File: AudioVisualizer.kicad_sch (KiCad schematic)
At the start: 327 parts, among them J1 AudioJack3, J2 AudioJack3, J3 Screw_Terminal_01x03, J4 USB_A, U1 LM2904, U10 LM393, U11 LM393, U12 LM393, U13 LM393, U14 LM393, U15 LM393, U16 LM393, U17 LM393, U18 LM393, U19 LM393, U2 LM2904, U20 LM393, U21 LM393, U22 LM393, U23 LM393, U24 LM393, U25 LM393, U26 LM393, U27 LM393, U28 LM393, U29 LM393, U3 LM2904, U30 LM393, U31 LM393, U32 LM393, U33 LM393, U34 LM393, U35 LM393, U36 LM393, U37 LM393, U38 LM393, U39 LM393, U4 LM2904, U40 LM393, U41 LM393, U42 LM393, U43 LM393, U44 LM393, U45 LM393, U46 LM393, U47 LM393, U48 LM393, U49 LM393, U5 LM2904, U50 LM393, U51 LM393, U52 LM393, U53 LM393, U54 L7805, U55 L7805, U6 LM393, U7 LM393, U8 LM393, U9 LM393

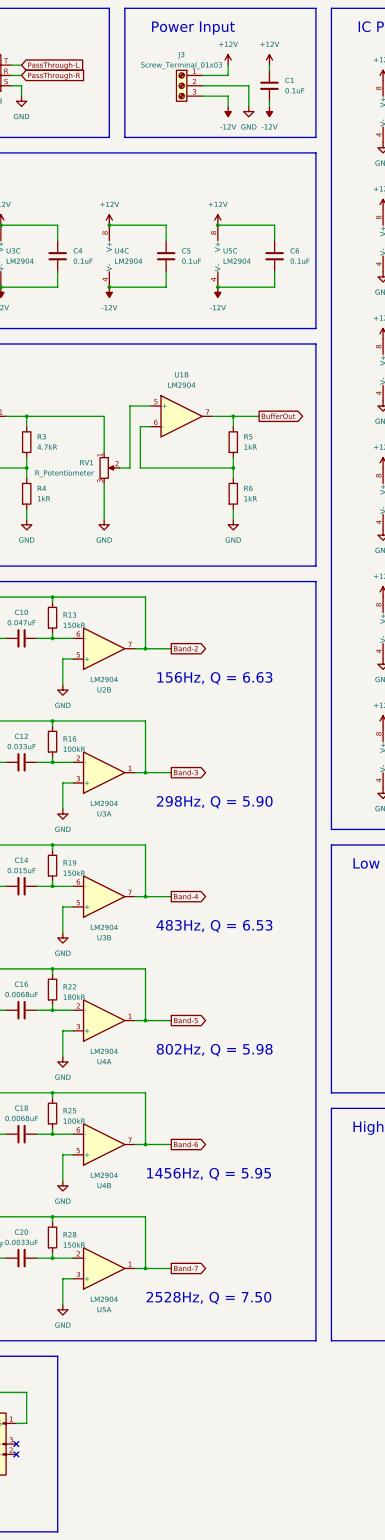
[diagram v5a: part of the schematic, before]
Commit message: 電源入力のパスコンを削除
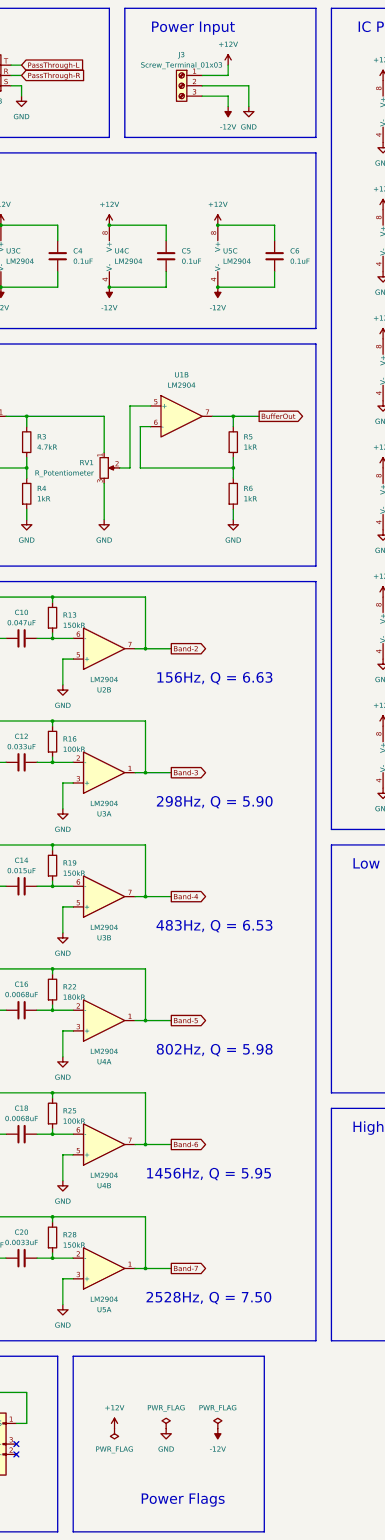
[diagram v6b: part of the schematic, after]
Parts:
- removed C1: 0.1uF, Capacitor_THT:C_Disc_D5.0mm_W2.5mm_P5.00mm, symbol Device:C
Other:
- note added: "Power Flags"
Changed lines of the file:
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@@
     (stroke (width 0) (type default))
   )
-  (wire (pts (xy 389.89 36.83) (xy 389.89 38.1))
-    (stroke (width 0) (type default))
-  )
   (wire (pts (xy 64.77 295.91) (xy 69.85 295.91))
     (stroke (width 0) (type default))
@@
     (stroke (width 0) (type default))
   )
-  (wire (pts (xy 389.89 45.72) (xy 389.89 46.99))
-    (stroke (width 0) (type default))
-  )
   (wire (pts (xy 538.48 170.18) (xy 558.8 170.18))
     (stroke (width 0) (type default))
@@
     (fill (type none))
   )
+  (rectangle (start 341.63 354.33) (end 388.62 397.51)
+    (stroke (width 0) (type default))
+    (fill (type none))
+  )
   (rectangle (start 265.43 354.33) (end 337.82 397.51)
     (stroke (width 0) (type default))
@@
     (effects (font (size 2.54 2.54)) (justify left bottom))
   )
+  (text "Power Flags" (at 358.14 391.16 0)
+    (effects (font (size 2.54 2.54)) (justify left bottom))
+  )
   (text "802Hz, Q = 5.98" (at 361.95 280.67 0)
     (effects (font (size 2.54 2.54)) (justify left bottom))
@@
     )
   )
+  (symbol (lib_id "power:GND") (at 364.49 372.11 0) (unit 1)
+    (in_bom yes) (on_board yes) (dnp no) (fields_autoplaced)
+    (property "Reference" "#PWR010" (at 364.49 378.46 0)
+      (effects (font (size 1.27 1.27)) hide)
+    )
+    (property "Value" "GND" (at 364.49 377.19 0)
+      (effects (font (size 1.27 1.27)))
+    )
+    (property "Footprint" "" (at 364.49 372.11 0)
+      (effects (font (size 1.27 1.27)) hide)
+    )
+    (property "Datasheet" "" (at 364.49 372.11 0)
+      (effects (font (size 1.27 1.27)) hide)
+    )
+    (pin "1")
+    (instances
+      (project "AudioVisualizer"
+        (path "/7f31d3f6-03f2-4f70-8f3a-2351ac21b94a"
+          (reference "#PWR010") (unit 1)
+        )
+      )
+    )
+  )
   (symbol (lib_id "Comparator:LM393") (at 223.52 269.24 0) (unit 2)
     (in_bom yes) (on_board yes) (dnp no) (fields_autoplaced)
@@
     )
   )
+  (symbol (lib_id "power:-12V") (at 377.19 372.11 180) (unit 1)
+    (in_bom yes) (on_board yes) (dnp no) (fields_autoplaced)
+    (property "Reference" "#PWR011" (at 377.19 374.65 0)
+      (effects (font (size 1.27 1.27)) hide)
+    )
+    (property "Value" "-12V" (at 377.19 377.19 0)
+      (effects (font (size 1.27 1.27)))
+    )
+    (property "Footprint" "" (at 377.19 372.11 0)
+      (effects (font (size 1.27 1.27)) hide)
+    )
+    (property "Datasheet" "" (at 377.19 372.11 0)
+      (effects (font (size 1.27 1.27)) hide)
+    )
+    (pin "1")
+    (instances
+      (project "AudioVisualizer"
+        (path "/7f31d3f6-03f2-4f70-8f3a-2351ac21b94a"
+          (reference "#PWR011") (unit 1)
+        )
+      )
+    )
+  )
   (symbol (lib_id "Device:LED") (at 248.92 223.52 0) (unit 1)
     (in_bom yes) (on_board yes) (dnp no) (fields_autoplaced)
@@
     )
   )
-  (symbol (lib_id "power:-12V") (at 389.89 46.99 180) (unit 1)
-    (in_bom yes) (on_board yes) (dnp no) (fields_autoplaced)
-    (property "Reference" "#PWR011" (at 389.89 49.53 0)
-      (effects (font (size 1.27 1.27)) hide)
-    )
-    (property "Value" "-12V" (at 389.89 52.07 0)
-      (effects (font (size 1.27 1.27)))
-    )
-    (property "Footprint" "" (at 389.89 46.99 0)
-      (effects (font (size 1.27 1.27)) hide)
-    )
-    (property "Datasheet" "" (at 389.89 46.99 0)
-      (effects (font (size 1.27 1.27)) hide)
-    )
-    (pin "1")
-    (instances
-      (project "AudioVisualizer"
-        (path "/7f31d3f6-03f2-4f70-8f3a-2351ac21b94a"
-          (reference "#PWR011") (unit 1)
-        )
-      )
-    )
-  )
   (symbol (lib_id "Comparator:LM393") (at 223.52 314.96 0) (unit 1)
     (in_bom yes) (on_board yes) (dnp no) (fields_autoplaced)
@@
     )
   )
+  (symbol (lib_id "power:+12V") (at 351.79 372.11 0) (unit 1)
+    (in_bom yes) (on_board yes) (dnp no) (fields_autoplaced)
+    (property "Reference" "#PWR0117" (at 351.79 375.92 0)
+      (effects (font (size 1.27 1.27)) hide)
+    )
+    (property "Value" "+12V" (at 351.79 367.03 0)
+      (effects (font (size 1.27 1.27)))
+    )
+    (property "Footprint" "" (at 351.79 372.11 0)
+      (effects (font (size 1.27 1.27)) hide)
+    )
+    (property "Datasheet" "" (at 351.79 372.11 0)
+      (effects (font (size 1.27 1.27)) hide)
+    )
+    (pin "1")
+    (instances
+      (project "AudioVisualizer"
+        (path "/7f31d3f6-03f2-4f70-8f3a-2351ac21b94a"
+          (reference "#PWR0117") (unit 1)
+        )
+      )
+    )
+  )
   (symbol (lib_id "Comparator:LM393") (at 106.68 220.98 0) (unit 1)
     (in_bom yes) (on_board yes) (dnp no) (fields_autoplaced)
@@
     )
   )
-  (symbol (lib_id "Device:C") (at 389.89 41.91 0) (unit 1)
-    (in_bom yes) (on_board yes) (dnp no) (fields_autoplaced)
-    (property "Reference" "C1" (at 393.7 40.64 0)
-      (effects (font (size 1.27 1.27)) (justify left))
-    )
-    (property "Value" "0.1uF" (at 393.7 43.18 0)
-      (effects (font (size 1.27 1.27)) (justify left))
-    )
-    (property "Footprint" "Capacitor_THT:C_Disc_D5.0mm_W2.5mm_P5.00mm" (at 390.8552 45.72 0)
-      (effects (font (size 1.27 1.27)) hide)
-    )
-    (property "Datasheet" "~" (at 389.89 41.91 0)
-      (effects (font (size 1.27 1.27)) hide)
-    )
-    (pin "1")
-    (pin "2")
-    (instances
-      (project "AudioVisualizer"
-        (path "/7f31d3f6-03f2-4f70-8f3a-2351ac21b94a"
-          (reference "C1") (unit 1)
-        )
-      )
-    )
-  )
   (symbol (lib_id "Regulator_Linear:L7805") (at 551.18 30.48 0) (unit 1)
     (in_bom yes) (on_board yes) (dnp no) (fields_autoplaced)
@@
     )
   )
+  (symbol (lib_id "power:PWR_FLAG") (at 364.49 372.11 0) (unit 1)
+    (in_bom yes) (on_board yes) (dnp no) (fields_autoplaced)
+    (property "Reference" "#FLG01" (at 364.49 370.205 0)
+      (effects (font (size 1.27 1.27)) hide)
+    )
+    (property "Value" "PWR_FLAG" (at 364.49 367.03 0)
+      (effects (font (size 1.27 1.27)))
+    )
+    (property "Footprint" "" (at 364.49 372.11 0)
+      (effects (font (size 1.27 1.27)) hide)
+    )
+    (property "Datasheet" "~" (at 364.49 372.11 0)
+      (effects (font (size 1.27 1.27)) hide)
+    )
+    (pin "1")
+    (instances
+      (project "AudioVisualizer"
+        (path "/7f31d3f6-03f2-4f70-8f3a-2351ac21b94a"
+          (reference "#FLG01") (unit 1)
+        )
+      )
+    )
+  )
   (symbol (lib_id "power:GND") (at 430.53 182.88 0) (unit 1)
     (in_bom yes) (on_board yes) (dnp no) (fields_autoplaced)
@@
     )
   )
+  (symbol (lib_id "power:PWR_FLAG") (at 377.19 372.11 0) (unit 1)
+    (in_bom yes) (on_board yes) (dnp no) (fields_autoplaced)
+    (property "Reference" "#FLG02" (at 377.19 370.205 0)
+      (effects (font (size 1.27 1.27)) hide)
+    )
+    (property "Value" "PWR_FLAG" (at 377.19 367.03 0)
+      (effects (font (size 1.27 1.27)))
+    )
+    (property "Footprint" "" (at 377.19 372.11 0)
+      (effects (font (size 1.27 1.27)) hide)
+    )
+    (property "Datasheet" "~" (at 377.19 372.11 0)
+      (effects (font (size 1.27 1.27)) hide)
+    )
+    (pin "1")
+    (instances
+      (project "AudioVisualizer"
+        (path "/7f31d3f6-03f2-4f70-8f3a-2351ac21b94a"
+          (reference "#FLG02") (unit 1)
+        )
+      )
+    )
+  )
   (symbol (lib_id "Comparator:LM393") (at 106.68 266.7 0) (unit 2)
     (in_bom yes) (on_board yes) (dnp no) (fields_autoplaced)
@@
     )
   )
+  (symbol (lib_id "power:PWR_FLAG") (at 351.79 372.11 180) (unit 1)
+    (in_bom yes) (on_board yes) (dnp no) (fields_autoplaced)
+    (property "Reference" "#FLG03" (at 351.79 374.015 0)
+      (effects (font (size 1.27 1.27)) hide)
+    )
+    (property "Value" "PWR_FLAG" (at 351.79 377.19 0)
+      (effects (font (size 1.27 1.27)))
+    )
+    (property "Footprint" "" (at 351.79 372.11 0)
+      (effects (font (size 1.27 1.27)) hide)
+    )
+    (property "Datasheet" "~" (at 351.79 372.11 0)
+      (effects (font (size 1.27 1.27)) hide)
+    )
+    (pin "1")
+    (instances
+      (project "AudioVisualizer"
+        (path "/7f31d3f6-03f2-4f70-8f3a-2351ac21b94a"
+          (reference "#FLG03") (unit 1)
+        )
+      )
+    )
+  )
   (symbol (lib_id "power:+5V") (at 138.43 186.69 0) (unit 1)
     (in_bom yes) (on_board yes) (dnp no) (fields_autoplaced)
@@
         )
       )
-    )
-  )
-  (symbol (lib_id "power:+12V") (at 389.89 36.83 0) (unit 1)
-    (in_bom yes) (on_board yes) (dnp no) (fields_autoplaced)
-    (property "Reference" "#PWR010" (at 389.89 40.64 0)
-      (effects (font (size 1.27 1.27)) hide)
-    )
-    (property "Value" "+12V" (at 389.89 31.75 0)
-      (effects (font (size 1.27 1.27)))
-    )
-    (property "Footprint" "" (at 389.89 36.83 0)
-      (effects (font (size 1.27 1.27)) hide)
-    )
-    (property "Datasheet" "" (at 389.89 36.83 0)
-      (effects (font (size 1.27 1.27)) hide)
-    )
-    (pin "1")
-    (instances
-      (project "AudioVisualizer"
-        (path "/7f31d3f6-03f2-4f70-8f3a-2351ac21b94a"
-          (reference "#PWR010") (unit 1)
-        )
-      )

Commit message: 少修正
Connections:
- net Filter_L_In: now also R2.1; no longer R1.1
- net Filter_R_In: now also R1.1; no longer R2.1
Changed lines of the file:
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@@
     )
   )
-  (global_label "Filter_L_In" (shape input) (at 285.75 116.84 180) (fields_autoplaced)
-    (effects (font (size 1.27 1.27)) (justify right))
-    (property "Intersheetrefs" "${INTERSHEET_REFS}" (at 273.0886 116.84 0)
+  (global_label "Filter_R_In" (shape input) (at 285.75 116.84 180) (fields_autoplaced)
+    (effects (font (size 1.27 1.27)) (justify right))
+    (property "Intersheetrefs" "${INTERSHEET_REFS}" (at 272.9261 116.84 0)
       (effects (font (size 1.27 1.27)) (justify right) hide)
     )
@@
     )
   )
-  (global_label "Filter_R_In" (shape input) (at 285.75 129.54 180) (fields_autoplaced)
-    (effects (font (size 1.27 1.27)) (justify right))
-    (property "Intersheetrefs" "${INTERSHEET_REFS}" (at 272.8467 129.54 0)
-      (effects (font (size 1.27 1.27)) (justify right) hide)
-    )
+  (global_label "Filter_L_In" (shape input) (at 285.75 129.54 180) (fields_autoplaced)
+    (effects (font (size 1.27 1.27)) (justify right))
+    (property "Intersheetrefs" "${INTERSHEET_REFS}" (at 273.168 129.54 0)
+      (effects (font (size 1.27 1.27)) (justify right) hide)
+    )
